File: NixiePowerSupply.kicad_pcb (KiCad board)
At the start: 2 copper layers, 22 parts, among them J1 BARREL_JACK, J2 CONN_01X04, J3 CONN_01X05, Q1 2SA1015, Q2 2SK3234, U1 NJM2360, U2 7805

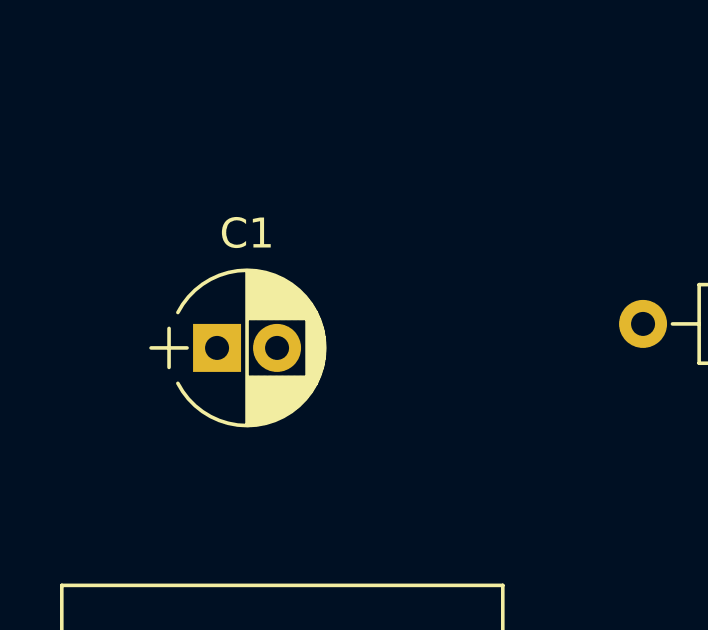
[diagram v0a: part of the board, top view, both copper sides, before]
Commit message: Add costed BOM
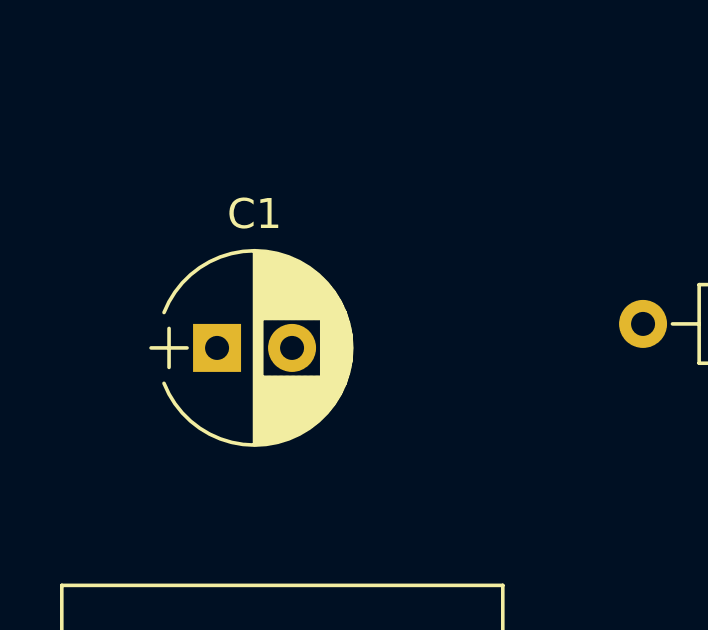
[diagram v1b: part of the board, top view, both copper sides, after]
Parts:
- C1: footprint Capacitors_THT:CP_Radial_D5.0mm_P2.00mm -> Capacitors_THT:CP_Radial_D6.3mm_P2.50mm

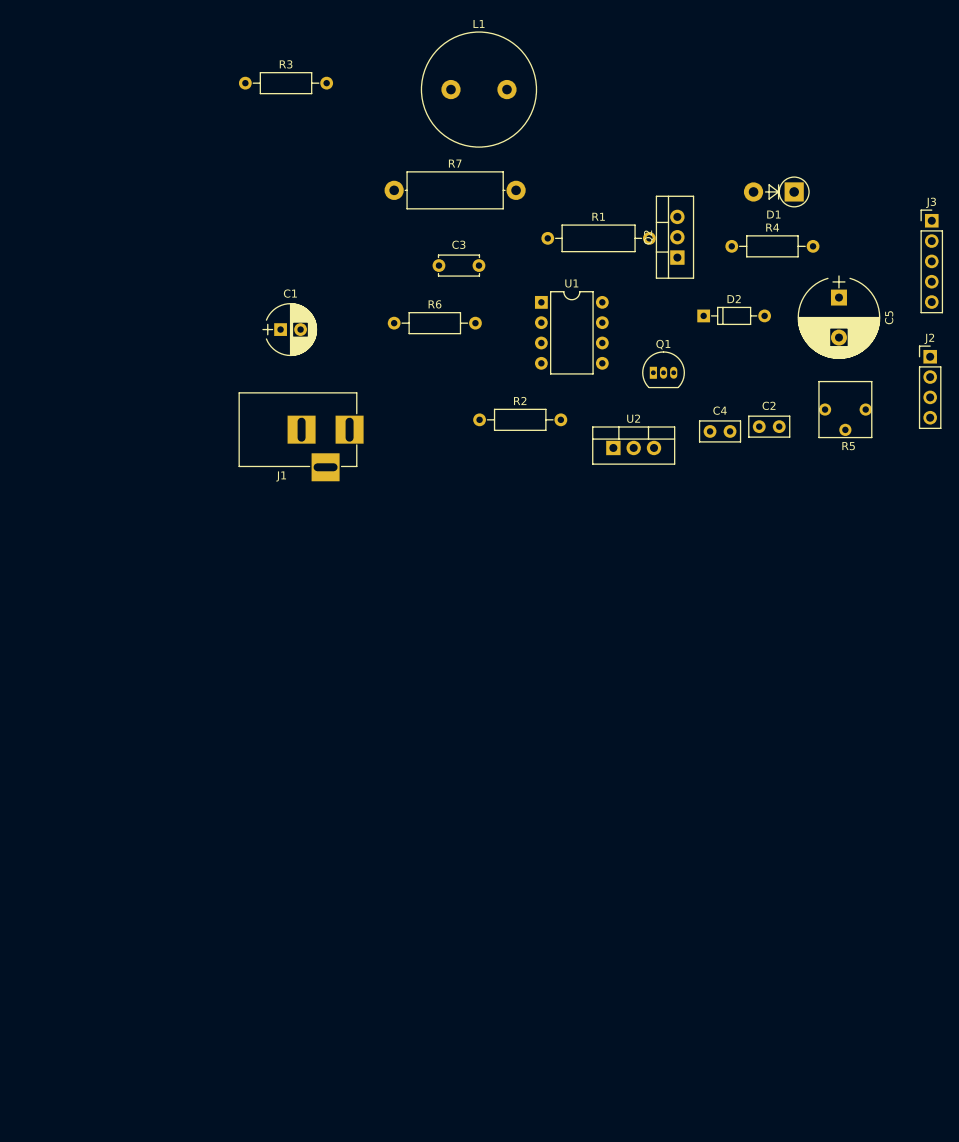
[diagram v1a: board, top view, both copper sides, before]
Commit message: Placement & Trace layoit done
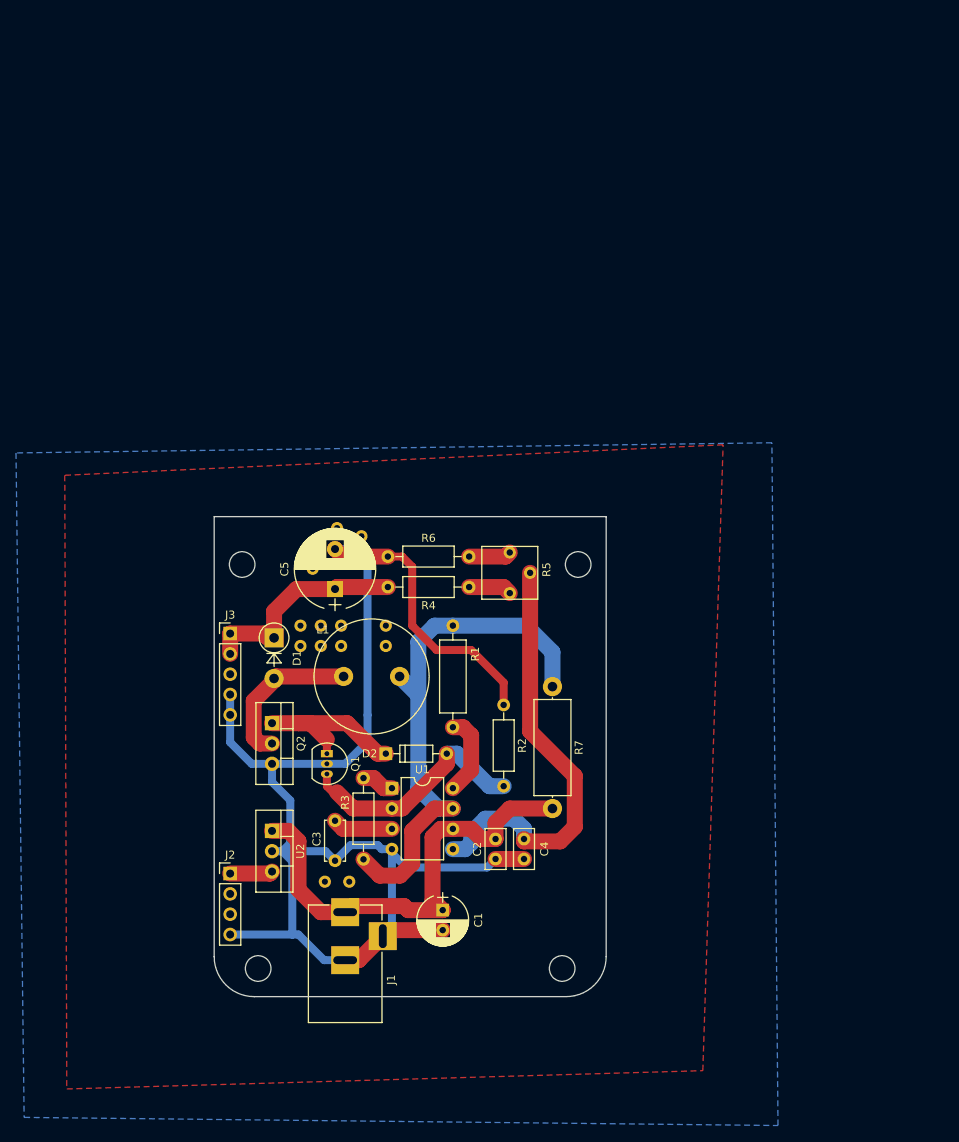
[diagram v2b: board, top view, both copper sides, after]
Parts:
- added REF**: , NixiePowerSupply:Via_Pad1mm_Hole0.6mm, F.Cu at (145.3, 96.0)
- added REF**: Via_Pad1mm_Hole0.6mm, NixiePowerSupply:Via_Pad1mm_Hole0.6mm, F.Cu at (150.4, 98.6)
- added REF**: Via_Pad1mm_Hole0.6mm, NixiePowerSupply:Via_Pad1mm_Hole0.6mm, F.Cu at (156.0, 96.0)
- added REF**: Via_Pad1mm_Hole0.6mm, NixiePowerSupply:Via_Pad1mm_Hole0.6mm, F.Cu at (156.0, 98.6)
- added REF**: Via_Pad1mm_Hole0.6mm, NixiePowerSupply:Via_Pad1mm_Hole0.6mm, F.Cu at (148.3, 128.0)
- added REF**: Via_Pad1mm_Hole0.6mm, NixiePowerSupply:Via_Pad1mm_Hole0.6mm, F.Cu at (151.4, 128.0)
- added REF**: Via_Pad1mm_Hole0.6mm, NixiePowerSupply:Via_Pad1mm_Hole0.6mm, F.Cu at (147.8, 96.0)
- added REF**: Via_Pad1mm_Hole0.6mm, NixiePowerSupply:Via_Pad1mm_Hole0.6mm, F.Cu at (145.3, 98.6)
- added REF**: Via_Pad1mm_Hole0.6mm, NixiePowerSupply:Via_Pad1mm_Hole0.6mm, F.Cu at (146.8, 86.4)
- added REF**: Via_Pad1mm_Hole0.6mm, NixiePowerSupply:Via_Pad1mm_Hole0.6mm, F.Cu at (146.8, 88.9)
- added REF**: Via_Pad1mm_Hole0.6mm, NixiePowerSupply:Via_Pad1mm_Hole0.6mm, F.Cu at (149.9, 83.8)
- added REF**: Via_Pad1mm_Hole0.6mm, NixiePowerSupply:Via_Pad1mm_Hole0.6mm, F.Cu at (152.9, 84.8)
- added REF**: Via_Pad1mm_Hole0.6mm, NixiePowerSupply:Via_Pad1mm_Hole0.6mm, F.Cu at (150.4, 96.0)
- added REF**: Via_Pad1mm_Hole0.6mm, NixiePowerSupply:Via_Pad1mm_Hole0.6mm, F.Cu at (147.8, 98.6)
- U2: value 7805 -> Regul_7805
- moved J2 108.8 mm to (136.5, 127.0)
- moved J3 101.8 mm to (136.5, 97.0)
- moved R3 88.1 mm to (153.2, 115.1), turned to 270 degrees
- moved D1 85.6 mm to (142.0, 97.5), turned to 270 degrees
- moved Q2 77.2 mm to (141.7, 108.2), turned to 270 degrees
- moved C1 75.3 mm to (163.1, 131.6), turned to 270 degrees
- moved L1 74.6 mm to (154.2, 102.4), turned to 180 degrees
- moved C5 72.8 mm to (149.6, 91.4), turned to 90 degrees
- moved C3 70.6 mm to (149.6, 120.4), turned to 270 degrees
- moved D2 67.6 mm to (156.0, 112.0)
- moved R7 65.1 mm to (176.8, 103.6), turned to 270 degrees
- moved U2 64.1 mm to (141.7, 121.7), turned to 270 degrees
- moved U1 63.5 mm to (156.7, 116.3)
- moved Q1 62.7 mm to (148.6, 112.0), turned to 270 degrees
- moved R1 62.3 mm to (164.3, 108.7), turned to 90 degrees
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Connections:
- J2 pad 2: Net-(J2-Pad2) -> (no net)
- J2 pad 3: Net-(J2-Pad3) -> (no net)
- J3 pad 3: Net-(J3-Pad3) -> (no net)
- U2 pad 1: (no net) -> +12V
- U2 pad 2: (no net) -> GND
- U2 pad 3: (no net) -> +5V
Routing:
- net GND: track 0.00 -> 187.5 mm
- net Net-(L1-Pad1): track 0.00 -> 68.1 mm
- net +12V: track 0.00 -> 58.0 mm
- net Net-(C4-Pad1): track 0.00 -> 54.5 mm
- net Net-(D2-Pad2): track 0.00 -> 30.0 mm
- net +HV: track 0.00 -> 27.0 mm
- net Net-(D2-Pad1): track 0.00 -> 22.0 mm
- net Net-(D1-Pad2): track 0.00 -> 19.8 mm
- net Net-(R1-Pad1): track 0.00 -> 10.3 mm
- net Net-(C3-Pad1): track 0.00 -> 7.53 mm
- net Net-(R4-Pad1): track 0.00 -> 5.40 mm
- net +5V: track 0.00 -> 5.34 mm
- net Net-(R5-Pad3): track 0.00 -> 5.29 mm
- net Net-(R3-Pad1): track 0.00 -> 4.08 mm
- added copper zone on B.Cu, net GND
- added copper zone on F.Cu, net GND
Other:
- board outline added: 49 x 60 mm
